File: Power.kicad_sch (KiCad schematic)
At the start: 18 parts, among them U2 TPS2116DRL, U4 TLV75733PDBV, U5 TPS62A02APDDC

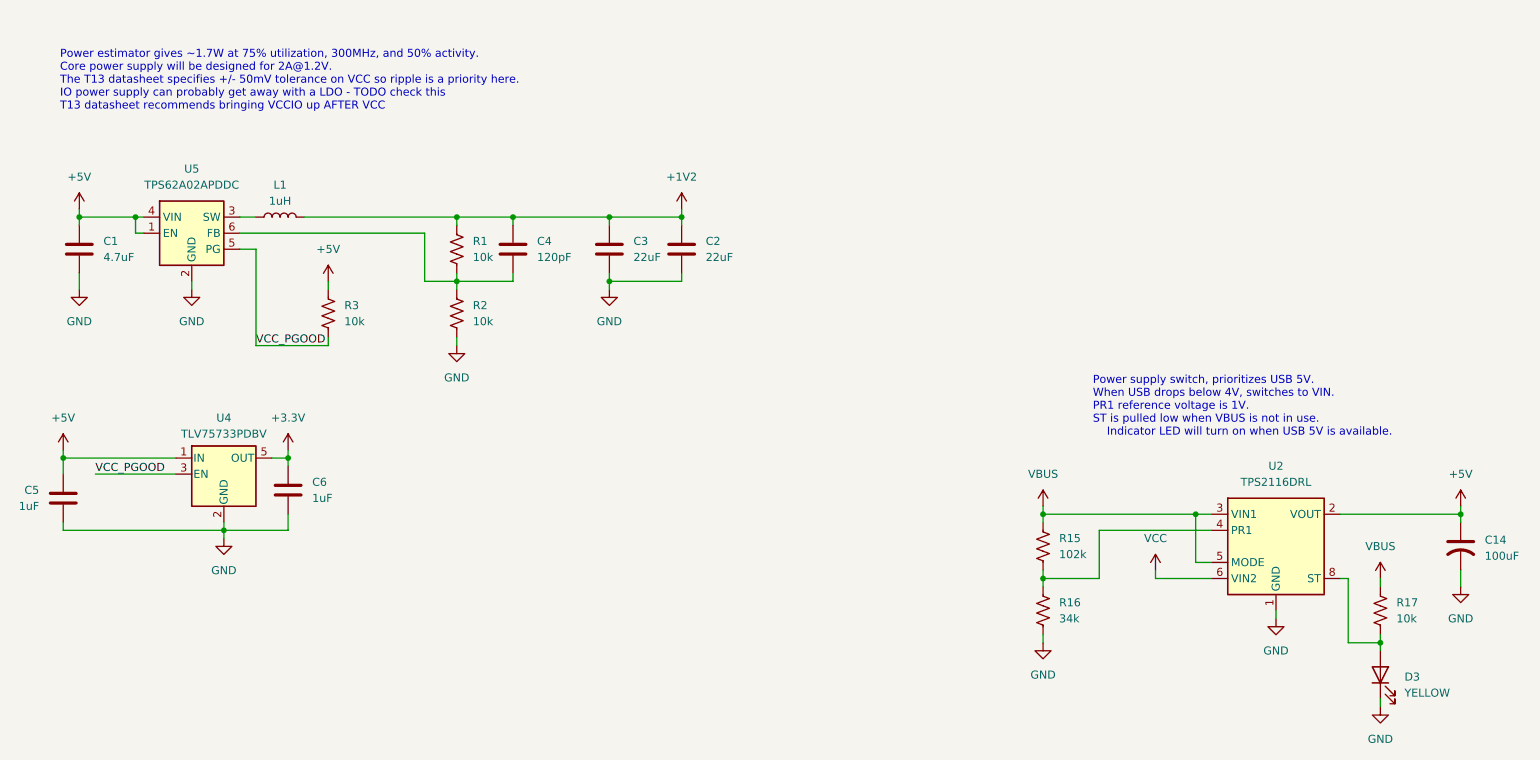
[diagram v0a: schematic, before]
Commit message: Added SRAM and removed old ADC
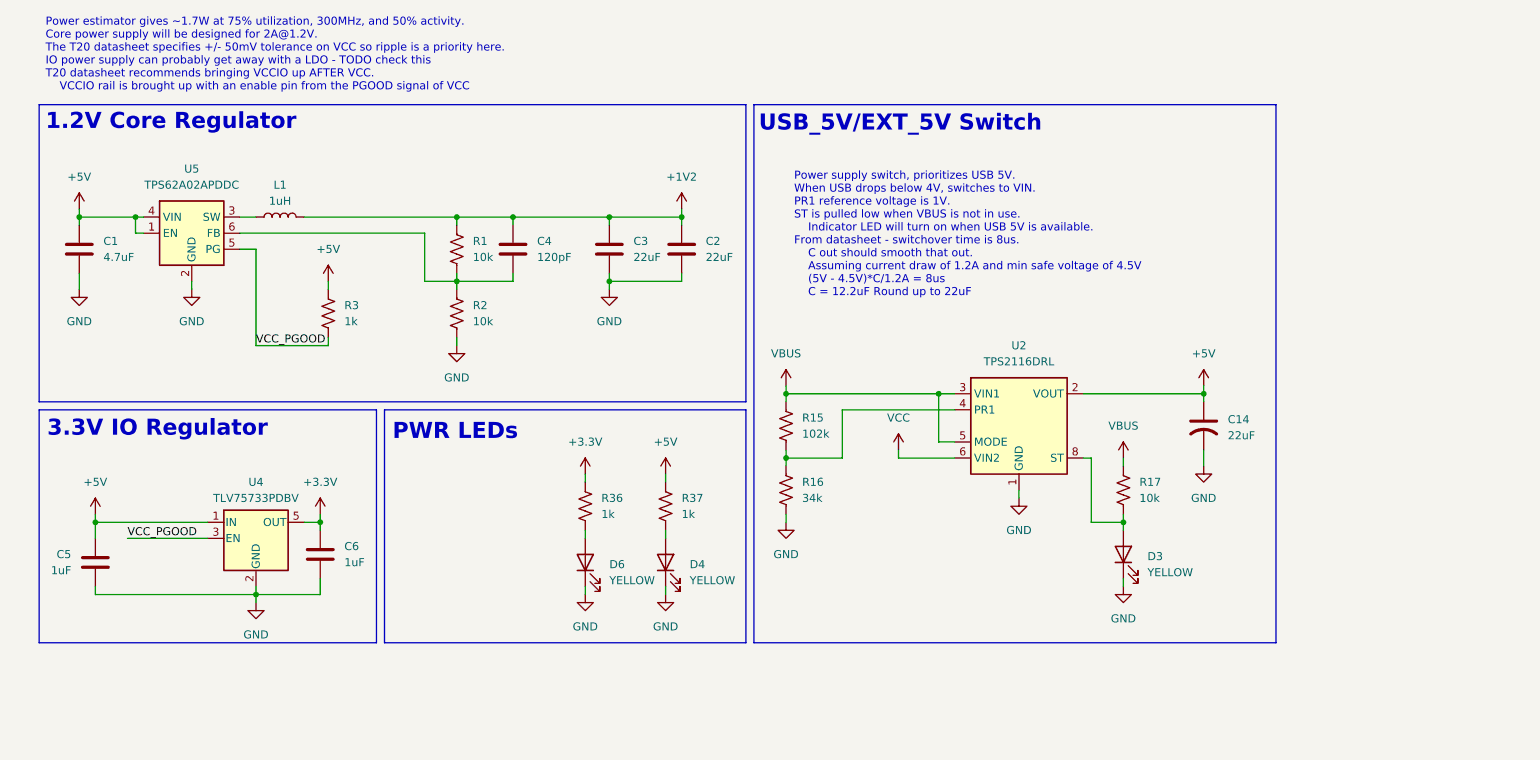
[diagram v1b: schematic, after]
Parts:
- added D4, D6: YELLOW, LED_SMD:LED_0603_1608Metric, symbol Device:LED
- added R36, R37: 1k, Resistor_SMD:R_0603_1608Metric, symbol Device:R_US
- C14: value 100uF -> 22uF
- R3: value 10k -> 1k
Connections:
- net +3.3V: now also R36.1
- net +5V: now also R37.1
- net GND: now also D4.1 (K), D6.1 (K)
- new net: D6.2 (A), R36.2
- new net: D4.2 (A), R37.2
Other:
- note added: "1.2V Core Regulator"
- note added: "3.3V IO Regulator"
- note added: "PWR LEDs"
- note added: "Power estimator gives ~1.7W at 75% utilization, 300MHz, and 50% activity. Core power supply will be designed for 2A@1.2V. The T20 datasheet specifies +/- 50mV tolerance on VCC so ripple is a priority here. IO power supply can probably get away with a LDO - TODO check this T20 datasheet recommends bringing VCCIO up AFTER VCC. VCCIO rail is brought up with an enable pin from the PGOOD signal of VCC"
- note added: "Power supply switch, prioritizes USB 5V. When USB drops below 4V, switches to VIN. PR1 reference voltage is 1V. ST is pulled low when VBUS is not in use. Indicator LED will turn on when USB 5V is available. From datasheet - switchover time is 8us. C out should smooth that out. Assuming current draw of 1.2A and min safe voltage of 4.5V (5V - 4.5V)*C/1.2A = 8us C = 12.2uF Round up to 22uF"
- note added: "USB_5V/EXT_5V Switch"
- note removed: "Power estimator gives ~1.7W at 75% utilization, 300MHz, and 50% activity. Core power supply will be designed for 2A@1.2V. The T13 datasheet specifies +/- 50mV tolerance on VCC so ripple is a priority here. IO power supply can probably get away with a LDO - TODO check this T13 datasheet recommends bringing VCCIO up AFTER VCC"
- note removed: "Power supply switch, prioritizes USB 5V. When USB drops below 4V, switches to VIN. PR1 reference voltage is 1V. ST is pulled low when VBUS is not in use. Indicator LED will turn on when USB 5V is available."
- moved on the sheet: C14, C5, C6, D3, R15, R16, R17, U2, U4

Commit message: Initial design
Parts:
- added TP21, TP22, TP23, TP24: TestPoint, TestPoint:TestPoint_Pad_D2.0mm, symbol Connector:TestPoint
- C1: footprint Capacitor_SMD:C_1206_3216Metric -> Capacitor_SMD:C_0603_1608Metric; Digikey PN (none) -> 1276-1044-1-ND; Unit Cost (none) -> 0.044
- C14: footprint Capacitor_THT:C_Radial_D6.3mm_H7.0mm_P2.50mm -> Capacitor_THT:C_Radial_D5.0mm_H7.0mm_P2.00mm; Digikey PN (none) -> P814-ND; Unit Cost (none) -> 0.27
- C2, C3: Digikey PN (none) -> 1276-2728-1-ND; Unit Cost (none) -> 0.29
- C4: value 120pF -> 20pF; Digikey PN (none) -> 1276-1187-1-ND; Unit Cost (none) -> 0.10
- C5, C6: Digikey PN (none) -> 1276-1859-1-ND; Unit Cost (none) -> 0.1
- D3, D4, D6: Digikey PN (none) -> 754-1124-1-ND; Unit Cost (none) -> 0.21
- L1: Digikey PN (none) -> 3526-WIP322512A-1R0MLDGCT-ND; Unit Cost (none) -> 0.11
- R1, R17, R2: Digikey PN (none) -> 311-10KLDCT-ND; Unit Cost (none) -> 0.028
- R15: Digikey PN (none) -> YAG1498CT-ND; Unit Cost (none) -> 0.11
- R16: Digikey PN (none) -> 311-34.0KHRCT-ND; Unit Cost (none) -> 0.11
- R3, R36, R37: Digikey PN (none) -> 311-1.00KHRCT-ND; Unit Cost (none) -> 0.025
- U2: Digikey PN (none) -> 296-TPS2116DRLRCT-ND; Unit Cost (none) -> 1.07
- U4: Digikey PN (none) -> 296-TLV75733PDYDRCT-ND; Unit Cost (none) -> 0.37
- U5: Digikey PN (none) -> 296-TPS62A02APDDCRCT-ND; Unit Cost (none) -> 0.24
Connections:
- net +1V2: now also TP21.1
- net +3.3V: now also TP22.1
- net +5V: now also TP23.1
- net VBUS: now also TP24.1

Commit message: Added ethernet
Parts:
- TP21, TP22, TP23, TP24: now left out of the parts list
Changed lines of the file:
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@@
 		(body_style 1)
 		(exclude_from_sim no)
-		(in_bom yes)
+		(in_bom no)
 		(on_board yes)
 		(in_pos_files yes)
@@
 		(body_style 1)
 		(exclude_from_sim no)
-		(in_bom yes)
+		(in_bom no)
 		(on_board yes)
 		(in_pos_files yes)
@@
 		(body_style 1)
 		(exclude_from_sim no)
-		(in_bom yes)
+		(in_bom no)
 		(on_board yes)
 		(in_pos_files yes)
@@
 		(body_style 1)
 		(exclude_from_sim no)
-		(in_bom yes)
+		(in_bom no)
 		(on_board yes)
 		(in_pos_files yes)

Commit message: Cleanup
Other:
- title: (none) -> Power
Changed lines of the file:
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@@
 	(generator_version "10.0")
 	(paper "A4")
+	(title_block
+		(title "Power")
+		(date "2026-09-19")
+	)
 	(rectangle
 		(start 93.98 100.33)

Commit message: Annotated schematic
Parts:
- renumbered C1 to C25, C5 to C26, C6 to C27, C4 to C28, C3 to C29, C2 to C30, C14 to C31, D6 to D4, D4 to D5, D3 to D6, R3 to R34, R1 to R35, R2 to R36, R36 to R37, R37 to R38, R15 to R39, R16 to R40, R17 to R41, TP22 to TP10, TP21 to TP11, TP24 to TP12, TP23 to TP13, U5 to U3, U2 to U5

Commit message: Started module-level layout
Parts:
- added C73: 4.7uF, Capacitor_SMD:C_0603_1608Metric, symbol Device:C
- C28: value 20pF -> 10pF; Digikey PN 1276-1187-1-ND -> 1276-2149-1-ND
- TP10, TP11, TP12, TP13: footprint TestPoint:TestPoint_Pad_D2.0mm -> TestPoint:TestPoint_Pad_D1.0mm
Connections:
- net +3.3V: now also C73.1
- net GND: now also C73.2
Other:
- moved on the sheet: C26, C27, TP10, U4

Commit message: Routing done
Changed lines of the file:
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@@
 		(lib_id "Connector:TestPoint")
 		(at 163.83 96.52 0)
+		(mirror y)
 		(unit 1)
 		(body_style 1)
@@
 		(dnp no)
 		(property "Reference" "TP12"
-			(at 165.354 90.678 0)
+			(at 162.306 90.678 0)
 			(show_name no)
 			(do_not_autoplace no)
@@
 		)
 		(property "Value" "TestPoint"
-			(at 161.29 91.9481 0)
+			(at 166.37 91.9481 0)
 			(hide yes)
 			(show_name no)
@@
 		)
 		(property "Footprint" "TestPoint:TestPoint_Pad_D1.0mm"
-			(at 168.91 96.52 0)
+			(at 158.75 96.52 0)
 			(hide yes)
 			(show_name no)
@@
 		)
 		(property "Datasheet" ""
-			(at 168.91 96.52 0)
+			(at 158.75 96.52 0)
 			(hide yes)
 			(show_name no)
